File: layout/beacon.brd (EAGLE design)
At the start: 25 x 40 mm, 24 parts, among them IC1 LP2985-SOT23-5, U1 BLE112-A

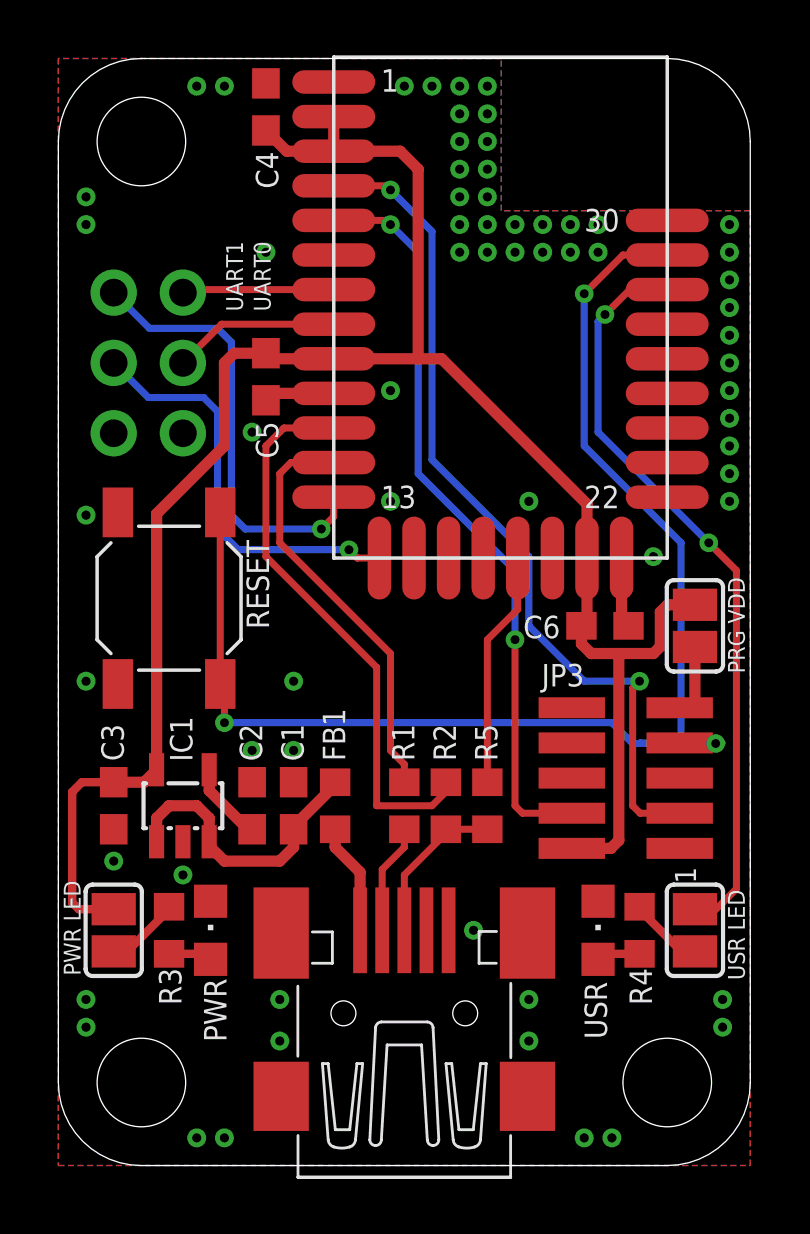
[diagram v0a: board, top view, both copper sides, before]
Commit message: Added battery option
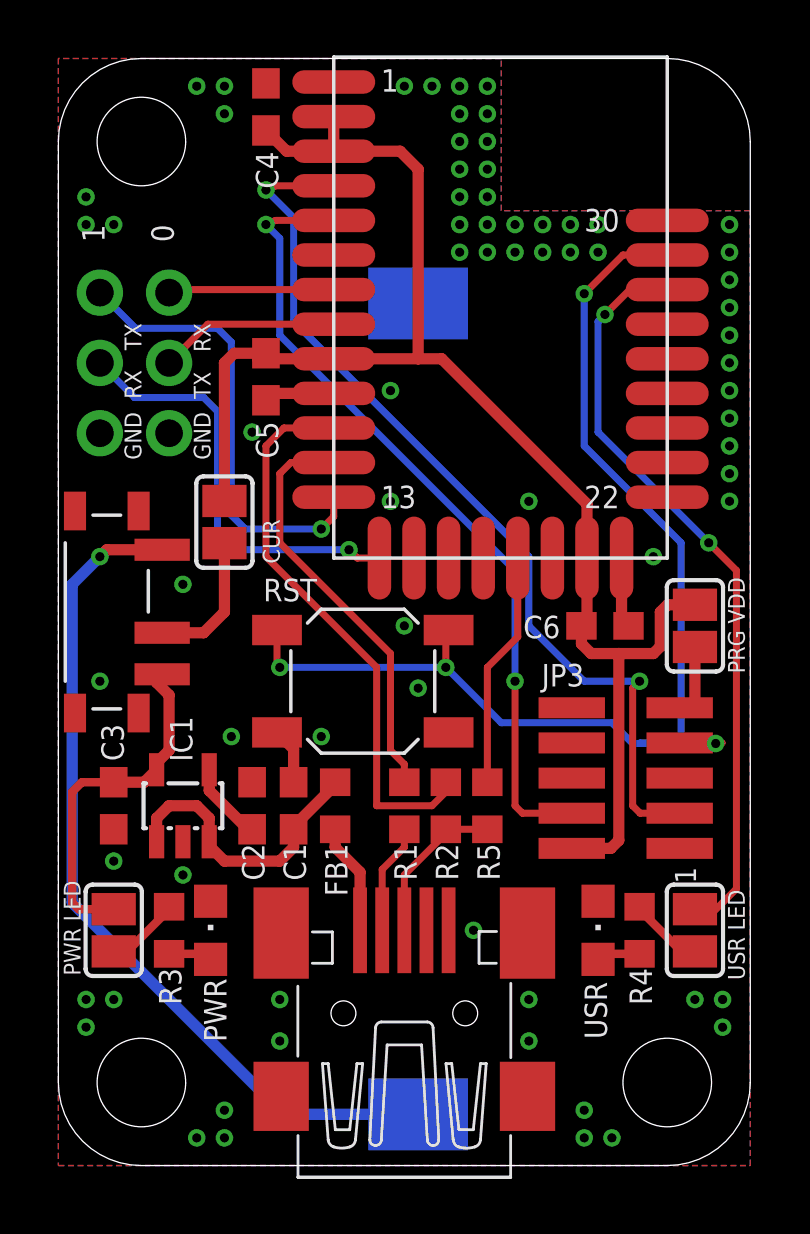
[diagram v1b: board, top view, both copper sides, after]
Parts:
- removed RESET: TACT-SWITCH-40-40, tactile-switch:40-40
- removed UART0, UART1: (no value), microbuilder:1X03_ROUND
- added 0, 1: (no value), microbuilder:1X03_ROUND
- added BT1: CR2032-HOLDER, battery-holder:CH28-2032LF
- added RST: TACT-SWITCH-40-40, tactile-switch:40-40
- added SJ4: PWR LED, jumper:SJ
- added U$1: 1P2T, switch:1P2T-ON-ON
- added U$2: (no value), pcb-artwork:JANIS_10MM
- added U$3: (no value), pcb-artwork:GITHUB/JAN1S
- added U$4: (no value), ohw-logo:OSHW_FILLX100_NOTEXT
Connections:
- new net N$4: SJ4.1, U$1.2
- new net VDD_BAT: BT1.POS, U$1.3
- new net VDD_USB: C3.1, IC1.5, SJ2.1, U$1.1
- net 3.3V: now also SJ4.2; no longer C3.1, IC1.5, SJ2.1
- net GND: now also 0.3, 1.3, BT1.NEG, RST.1, RST.2; no longer RESET.1, RESET.2, UART0.3, UART1.3
- net P1_4: now also 1.2; no longer UART1.2
- net P1_5: now also 1.1; no longer UART1.1
- net P1_6: now also 0.2; no longer UART0.2
- net P1_7: now also 0.1; no longer UART0.1
- net RESET: now also RST.3, RST.4; no longer RESET.3, RESET.4
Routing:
- net VDD_BAT: track 0.00 -> 30.9 mm, vias 0 -> 1
- net 3.3V: track 74.4 -> 54.7 mm
- net VDD_USB: track 0.00 -> 13.0 mm
- net RESET: track 51.6 -> 45.5 mm, vias 3 -> 4
- net N$4: track 0.00 -> 5.05 mm
- net P2_2: track 31.2 -> 33.4 mm
- net P2_1: track 27.1 -> 29.4 mm
- net GND: track 5.17 -> 7.21 mm, vias 65 -> 71
- net P1_7: track 5.47 -> 5.97 mm
- net P1_6: track 6.03 -> 6.53 mm
- net P1_5: track 16.0 -> 16.5 mm
- net P1_4: track 15.0 -> 15.5 mm
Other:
- board text added: "CUR"
- board text added: "GND RX TX"
- board text added: "GND TX RX"
- board text added: "USB <-> BAT"

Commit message: Minor fix
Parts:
- moved U$4 19.7 mm to (22.0, 8.00), turned to 90 degrees
- moved U$3 12.6 mm to (22.5, 11.5), turned to 90 degrees
- moved U$2 0.90 mm to (23.5, 29.5)
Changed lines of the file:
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@@
 </classes>
 <designrules>
+<description language="de">&lt;b&gt;EAGLE Design-Regeln&lt;/b&gt;
+&lt;p&gt;
+Die Standard-Design-Regeln sind so gewählt, dass sie für
+die meisten Anwendungen passen. Sollte ihre Platine
+besondere Anforderungen haben, treffen Sie die erforderlichen
+Einstellungen hier und speichern die Design-Regeln unter
+einem neuen Namen ab.
+</description>
 <description language="en">&lt;b&gt;Dirty Cheap Dirty Board Design Rules&lt;/b&gt;
 &lt;br&gt;
@@
 <attribute name="VALUE" x="6" y="23.6501" size="0.02" layer="27" rot="R90"/>
 </element>
-<element name="U$2" library="pcb-artwork" package="JANIS_10MM" value="" x="22.75" y="29" rot="MR0"/>
-<element name="U$3" library="pcb-artwork" package="GITHUB/JAN1S" value="" x="24" y="24" rot="MR270"/>
-<element name="U$4" library="ohw-logo" package="OSHW_FILLX100_NOTEXT" value="" x="24.5" y="27.5" rot="MR270"/>
+<element name="U$4" library="ohw-logo" package="OSHW_FILLX100_NOTEXT" value="" x="22" y="8" rot="MR90"/>
+<element name="U$2" library="pcb-artwork" package="JANIS_10MM" value="" x="23.5" y="29.5" rot="MR0"/>
+<element name="U$3" library="pcb-artwork" package="GITHUB/JAN1S" value="" x="22.5" y="11.5" rot="MR90"/>
 </elements>
 <signals>
